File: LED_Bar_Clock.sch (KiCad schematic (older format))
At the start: 51 parts, among them J2 AVR-ISP-6, SW1 SKHMQKE010, SW2 SW_5_Way, U1 ATtiny84A-SSUR, U2 DS1307Z+, Y1 32.768 kHz

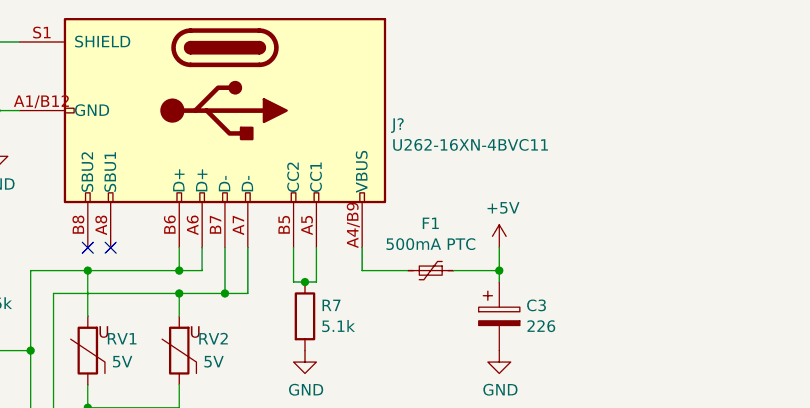
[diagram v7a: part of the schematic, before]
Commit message: annotate usb receptacle and regen netlist
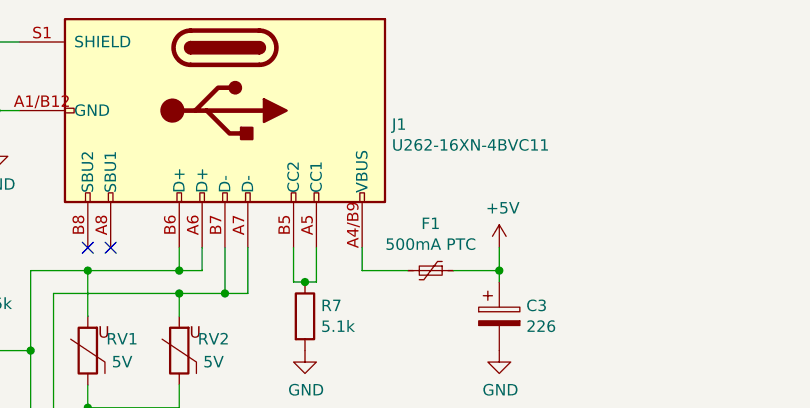
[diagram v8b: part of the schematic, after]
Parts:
- gave numbers to parts that had none: 1
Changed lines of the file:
@@
 $EndComp
 $Comp
-L Clock_Symbols:U262-16XN-4BVC11 J?
+L Clock_Symbols:U262-16XN-4BVC11 J1
 U 1 1 5CC92605
 P 3900 1150
-F 0 "J?" V 3961 1880 50  0000 L CNN
+F 0 "J1" V 3961 1880 50  0000 L CNN
 F 1 "U262-16XN-4BVC11" V 4052 1880 50  0000 L CNN
 F 2 "Clock_Footprints:U262-16XN-4BVC11" H 4050 1150 50  0001 C CNN
